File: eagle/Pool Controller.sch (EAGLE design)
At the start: 23 parts, among them J1 POWER_JACKPTH, J2 Temp_Pool, J3 Relay, J4 Solar_Mon, J5 Temp_Solar

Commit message: Updated Eagle Files
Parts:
- S4: value Solar_Toggle -> Display Step
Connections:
- new net N$10: R10.2, S2.3, S2.4
- new net N$13: R8.2, S4.3, S4.4
- new net N$15: R6.2, S1.3, S1.4
- new net VCC: R4.P$1
- net 3.3V: no longer R5.1
- net GND: now also R5.1; no longer R4.P$1
- net N$8: no longer R10.2, R6.2, R8.2, S1.3, S1.4, S2.3, S2.4, S4.3, S4.4
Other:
- note added: "2.1"
- note removed: "2.0.0"
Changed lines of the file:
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@@
 <part name="S2" library="SparkFun-Retired" deviceset="TAC_SWITCH" device="PTH" value="Clean"/>
 <part name="S3" library="SparkFun-Retired" deviceset="TAC_SWITCH" device="PTH" value="Stop"/>
-<part name="S4" library="SparkFun-Retired" deviceset="TAC_SWITCH" device="PTH" value="Solar_Toggle"/>
+<part name="S4" library="SparkFun-Retired" deviceset="TAC_SWITCH" device="PTH" value="Display Step"/>
 <part name="R10" library="SparkFun-Passives" deviceset="RESISTOR" device="AXIAL-0.3" value="22KΩ"/>
 <part name="J3" library="SparkFun-Connectors" deviceset="M06" device="SILK_FEMALE_PTH" value="Relay"/>
@@
 <sheet>
 <plain>
-<text x="233.68" y="-38.1" size="1.778" layer="97">2.0.0</text>
+<text x="233.68" y="-38.1" size="1.778" layer="97">2.1</text>
 </plain>
 <instances>
@@
 <instance part="GND4" gate="1" x="182.88" y="40.64" rot="R180"/>
 <instance part="SUPPLY4" gate="G$1" x="132.08" y="43.18"/>
-<instance part="SUPPLY5" gate="G$1" x="53.34" y="55.88"/>
-<instance part="GND6" gate="1" x="53.34" y="68.58"/>
+<instance part="SUPPLY5" gate="G$1" x="53.34" y="73.66"/>
+<instance part="GND6" gate="1" x="53.34" y="50.8"/>
 <instance part="SUPPLY6" gate="G$1" x="27.94" y="127"/>
 <instance part="SUPPLY7" gate="G$1" x="187.96" y="38.1"/>
@@
 </segment>
 <segment>
-<pinref part="GND6" gate="1" pin="GND"/>
-<pinref part="R4" gate="G$1" pin="P$1"/>
-<wire x1="53.34" y1="71.12" x2="60.96" y2="71.12" width="0.1524" layer="91"/>
-</segment>
-<segment>
 <pinref part="U$1" gate="G$1" pin="GND@21"/>
 <wire x1="165.1" y1="93.98" x2="180.34" y2="93.98" width="0.1524" layer="91"/>
@@
 <pinref part="J5" gate="G$1" pin="2"/>
 <wire x1="96.52" y1="73.66" x2="93.98" y2="73.66" width="0.1524" layer="91"/>
+</segment>
+<segment>
+<pinref part="R5" gate="G$1" pin="1"/>
+<wire x1="60.96" y1="55.88" x2="53.34" y2="55.88" width="0.1524" layer="91"/>
+<pinref part="GND6" gate="1" pin="GND"/>
+<wire x1="53.34" y1="55.88" x2="53.34" y2="53.34" width="0.1524" layer="91"/>
 </segment>
 </net>
@@
 <net name="N$8" class="0">
 <segment>
-<pinref part="R8" gate="G$1" pin="2"/>
 <pinref part="R7" gate="G$1" pin="2"/>
-<wire x1="114.3" y1="-17.78" x2="114.3" y2="0" width="0.1524" layer="91"/>
-<pinref part="R6" gate="G$1" pin="2"/>
-<wire x1="114.3" y1="0" x2="114.3" y2="20.32" width="0.1524" layer="91"/>
-<junction x="114.3" y="0"/>
-<pinref part="R10" gate="G$1" pin="2"/>
-<wire x1="114.3" y1="20.32" x2="114.3" y2="38.1" width="0.1524" layer="91"/>
-<junction x="114.3" y="20.32"/>
-<pinref part="S2" gate="S" pin="4"/>
-<wire x1="109.22" y1="17.78" x2="111.76" y2="17.78" width="0.1524" layer="91"/>
-<wire x1="111.76" y1="17.78" x2="111.76" y2="20.32" width="0.1524" layer="91"/>
-<wire x1="111.76" y1="20.32" x2="114.3" y2="20.32" width="0.1524" layer="91"/>
-<pinref part="S2" gate="S" pin="3"/>
-<wire x1="109.22" y1="20.32" x2="111.76" y2="20.32" width="0.1524" layer="91"/>
-<junction x="111.76" y="20.32"/>
-<pinref part="S1" gate="S" pin="4"/>
-<wire x1="109.22" y1="35.56" x2="111.76" y2="35.56" width="0.1524" layer="91"/>
-<wire x1="111.76" y1="35.56" x2="111.76" y2="38.1" width="0.1524" layer="91"/>
-<wire x1="111.76" y1="38.1" x2="114.3" y2="38.1" width="0.1524" layer="91"/>
-<junction x="114.3" y="38.1"/>
-<pinref part="S1" gate="S" pin="3"/>
-<wire x1="109.22" y1="38.1" x2="111.76" y2="38.1" width="0.1524" layer="91"/>
-<junction x="111.76" y="38.1"/>
 <pinref part="S3" gate="S" pin="4"/>
 <wire x1="109.22" y1="-2.54" x2="111.76" y2="-2.54" width="0.1524" layer="91"/>
@@
 <wire x1="109.22" y1="0" x2="111.76" y2="0" width="0.1524" layer="91"/>
 <junction x="111.76" y="0"/>
-<pinref part="S4" gate="S" pin="4"/>
-<wire x1="109.22" y1="-20.32" x2="111.76" y2="-20.32" width="0.1524" layer="91"/>
-<wire x1="111.76" y1="-20.32" x2="111.76" y2="-17.78" width="0.1524" layer="91"/>
-<wire x1="111.76" y1="-17.78" x2="114.3" y2="-17.78" width="0.1524" layer="91"/>
-<junction x="114.3" y="-17.78"/>
-<pinref part="S4" gate="S" pin="3"/>
-<wire x1="109.22" y1="-17.78" x2="111.76" y2="-17.78" width="0.1524" layer="91"/>
-<junction x="111.76" y="-17.78"/>
 </segment>
 </net>
@@
 </segment>
 <segment>
-<pinref part="R5" gate="G$1" pin="1"/>
-<pinref part="SUPPLY5" gate="G$1" pin="VCC"/>
-<wire x1="60.96" y1="55.88" x2="53.34" y2="55.88" width="0.1524" layer="91"/>
-</segment>
-<segment>
 <pinref part="SUPPLY10" gate="G$1" pin="VCC"/>
 <wire x1="213.36" y1="104.14" x2="213.36" y2="96.52" width="0.1524" layer="91"/>
@@
 </segment>
 </net>
+<net name="VCC" class="0">
+<segment>
+<pinref part="R4" gate="G$1" pin="P$1"/>
+<wire x1="60.96" y1="71.12" x2="53.34" y2="71.12" width="0.1524" layer="91"/>
+<pinref part="SUPPLY5" gate="G$1" pin="VCC"/>
+<wire x1="53.34" y1="71.12" x2="53.34" y2="73.66" width="0.1524" layer="91"/>
+</segment>
+</net>
+<net name="N$15" class="0">
+<segment>
+<pinref part="R6" gate="G$1" pin="2"/>
+<wire x1="111.76" y1="38.1" x2="114.3" y2="38.1" width="0.1524" layer="91"/>
+<pinref part="S1" gate="S" pin="3"/>
+<wire x1="109.22" y1="38.1" x2="111.76" y2="38.1" width="0.1524" layer="91"/>
+<junction x="111.76" y="38.1"/>
+<wire x1="111.76" y1="35.56" x2="111.76" y2="38.1" width="0.1524" layer="91"/>
+<pinref part="S1" gate="S" pin="4"/>
+<wire x1="109.22" y1="35.56" x2="111.76" y2="35.56" width="0.1524" layer="91"/>
+</segment>
+</net>
+<net name="N$10" class="0">
+<segment>
+<pinref part="R10" gate="G$1" pin="2"/>
+<wire x1="111.76" y1="20.32" x2="114.3" y2="20.32" width="0.1524" layer="91"/>
+<pinref part="S2" gate="S" pin="3"/>
+<wire x1="109.22" y1="20.32" x2="111.76" y2="20.32" width="0.1524" layer="91"/>
+<junction x="111.76" y="20.32"/>
+<wire x1="111.76" y1="17.78" x2="111.76" y2="20.32" width="0.1524" layer="91"/>
+<pinref part="S2" gate="S" pin="4"/>
+<wire x1="109.22" y1="17.78" x2="111.76" y2="17.78" width="0.1524" layer="91"/>
+</segment>
+</net>
+<net name="N$13" class="0">
+<segment>
+<pinref part="R8" gate="G$1" pin="2"/>
+<wire x1="111.76" y1="-17.78" x2="114.3" y2="-17.78" width="0.1524" layer="91"/>
+<pinref part="S4" gate="S" pin="3"/>
+<wire x1="109.22" y1="-17.78" x2="111.76" y2="-17.78" width="0.1524" layer="91"/>
+<junction x="111.76" y="-17.78"/>
+<wire x1="111.76" y1="-20.32" x2="111.76" y2="-17.78" width="0.1524" layer="91"/>
+<pinref part="S4" gate="S" pin="4"/>
+<wire x1="109.22" y1="-20.32" x2="111.76" y2="-20.32" width="0.1524" layer="91"/>
+</segment>
+</net>

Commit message: Finished initial design
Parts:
- renumbered U$1 to POOL_CONTROLLER
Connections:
- removed net VCC: R4.P$1
- net 3.3V: now also R4.P$1
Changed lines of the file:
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@@
 </classes>
 <parts>
-<part name="U$1" library="Spark" deviceset="PHOTON" device="_WITH_HEADERS"/>
+<part name="POOL_CONTROLLER" library="Spark" deviceset="PHOTON" device="_WITH_HEADERS"/>
 <part name="U$2" library="tft_1.8_1.44_oled_0.96" deviceset="OLED_0.96_I2C" device=""/>
 <part name="FRAME1" library="frames" deviceset="LETTER_L" device=""/>
@@
 </plain>
 <instances>
-<instance part="U$1" gate="G$1" x="147.32" y="81.28"/>
+<instance part="POOL_CONTROLLER" gate="G$1" x="147.32" y="81.28"/>
 <instance part="U$2" gate="G$1" x="177.8" y="20.32" rot="R180"/>
 <instance part="FRAME1" gate="G$1" x="-5.08" y="-45.72"/>
@@
 </segment>
 <segment>
-<pinref part="U$1" gate="G$1" pin="GND@21"/>
+<pinref part="POOL_CONTROLLER" gate="G$1" pin="GND@21"/>
 <wire x1="165.1" y1="93.98" x2="180.34" y2="93.98" width="0.1524" layer="91"/>
 <wire x1="180.34" y1="93.98" x2="180.34" y2="99.06" width="0.1524" layer="91"/>
@@
 </segment>
 <segment>
-<pinref part="U$1" gate="G$1" pin="GND@2"/>
+<pinref part="POOL_CONTROLLER" gate="G$1" pin="GND@2"/>
 <pinref part="GND2" gate="1" pin="GND"/>
 <wire x1="129.54" y1="104.14" x2="121.92" y2="104.14" width="0.1524" layer="91"/>
@@
 <net name="N$3" class="0">
 <segment>
-<pinref part="U$1" gate="G$1" pin="D0"/>
+<pinref part="POOL_CONTROLLER" gate="G$1" pin="D0"/>
 <wire x1="165.1" y1="53.34" x2="175.26" y2="53.34" width="0.1524" layer="91"/>
 <pinref part="U$2" gate="G$1" pin="SDA"/>
@@
 <net name="N$4" class="0">
 <segment>
-<pinref part="U$1" gate="G$1" pin="D1"/>
+<pinref part="POOL_CONTROLLER" gate="G$1" pin="D1"/>
 <wire x1="165.1" y1="58.42" x2="177.8" y2="58.42" width="0.1524" layer="91"/>
 <pinref part="U$2" gate="G$1" pin="SCL"/>
@@
 <net name="N$5" class="0">
 <segment>
-<pinref part="U$1" gate="G$1" pin="A1"/>
+<pinref part="POOL_CONTROLLER" gate="G$1" pin="A1"/>
 <wire x1="129.54" y1="58.42" x2="76.2" y2="58.42" width="0.1524" layer="91"/>
 <pinref part="R4" gate="G$1" pin="P$2"/>
@@
 <net name="N$1" class="0">
 <segment>
-<pinref part="U$1" gate="G$1" pin="D2"/>
+<pinref part="POOL_CONTROLLER" gate="G$1" pin="D2"/>
 <wire x1="165.1" y1="63.5" x2="213.36" y2="63.5" width="0.1524" layer="91"/>
 <wire x1="213.36" y1="63.5" x2="213.36" y2="66.04" width="0.1524" layer="91"/>
@@
 <net name="N$2" class="0">
 <segment>
-<pinref part="U$1" gate="G$1" pin="D3"/>
+<pinref part="POOL_CONTROLLER" gate="G$1" pin="D3"/>
 <wire x1="165.1" y1="68.58" x2="218.44" y2="68.58" width="0.1524" layer="91"/>
 <pinref part="J3" gate="G$1" pin="4"/>
@@
 <net name="N$7" class="0">
 <segment>
-<pinref part="U$1" gate="G$1" pin="D5"/>
+<pinref part="POOL_CONTROLLER" gate="G$1" pin="D5"/>
 <wire x1="165.1" y1="78.74" x2="213.36" y2="78.74" width="0.1524" layer="91"/>
 <wire x1="213.36" y1="78.74" x2="213.36" y2="73.66" width="0.1524" layer="91"/>
@@
 <net name="N$9" class="0">
 <segment>
-<pinref part="U$1" gate="G$1" pin="D6"/>
+<pinref part="POOL_CONTROLLER" gate="G$1" pin="D6"/>
 <wire x1="165.1" y1="83.82" x2="213.36" y2="83.82" width="0.1524" layer="91"/>
 <wire x1="213.36" y1="83.82" x2="213.36" y2="93.98" width="0.1524" layer="91"/>
@@
 <wire x1="96.52" y1="38.1" x2="96.52" y2="53.34" width="0.1524" layer="91"/>
 <junction x="96.52" y="38.1"/>
-<pinref part="U$1" gate="G$1" pin="A0"/>
+<pinref part="POOL_CONTROLLER" gate="G$1" pin="A0"/>
 <wire x1="96.52" y1="53.34" x2="129.54" y2="53.34" width="0.1524" layer="91"/>
 </segment>
@@
 <pinref part="J3" gate="G$1" pin="3"/>
 <wire x1="210.82" y1="71.12" x2="218.44" y2="71.12" width="0.1524" layer="91"/>
-<pinref part="U$1" gate="G$1" pin="D4"/>
+<pinref part="POOL_CONTROLLER" gate="G$1" pin="D4"/>
 <wire x1="165.1" y1="73.66" x2="210.82" y2="73.66" width="0.1524" layer="91"/>
 </segment>
@@
 <wire x1="104.14" y1="71.12" x2="111.76" y2="71.12" width="0.1524" layer="91"/>
 <wire x1="111.76" y1="71.12" x2="111.76" y2="63.5" width="0.1524" layer="91"/>
-<pinref part="U$1" gate="G$1" pin="A2"/>
+<pinref part="POOL_CONTROLLER" gate="G$1" pin="A2"/>
 <wire x1="111.76" y1="63.5" x2="129.54" y2="63.5" width="0.1524" layer="91"/>
 <pinref part="R14" gate="G$1" pin="2"/>
@@
 <segment>
 <wire x1="114.3" y1="86.36" x2="114.3" y2="68.58" width="0.1524" layer="91"/>
-<pinref part="U$1" gate="G$1" pin="A3"/>
+<pinref part="POOL_CONTROLLER" gate="G$1" pin="A3"/>
 <wire x1="114.3" y1="68.58" x2="129.54" y2="68.58" width="0.1524" layer="91"/>
 <pinref part="J2" gate="G$1" pin="1"/>
@@
 </segment>
 <segment>
-<pinref part="U$1" gate="G$1" pin="3V3"/>
+<pinref part="POOL_CONTROLLER" gate="G$1" pin="3V3"/>
 <wire x1="165.1" y1="109.22" x2="175.26" y2="109.22" width="0.1524" layer="91"/>
 <pinref part="SUPPLY2" gate="G$1" pin="VCC"/>
@@
 <wire x1="104.14" y1="101.6" x2="104.14" y2="106.68" width="0.1524" layer="91"/>
 </segment>
-</net>
-<net name="VCC" class="0">
 <segment>
 <pinref part="R4" gate="G$1" pin="P$1"/>

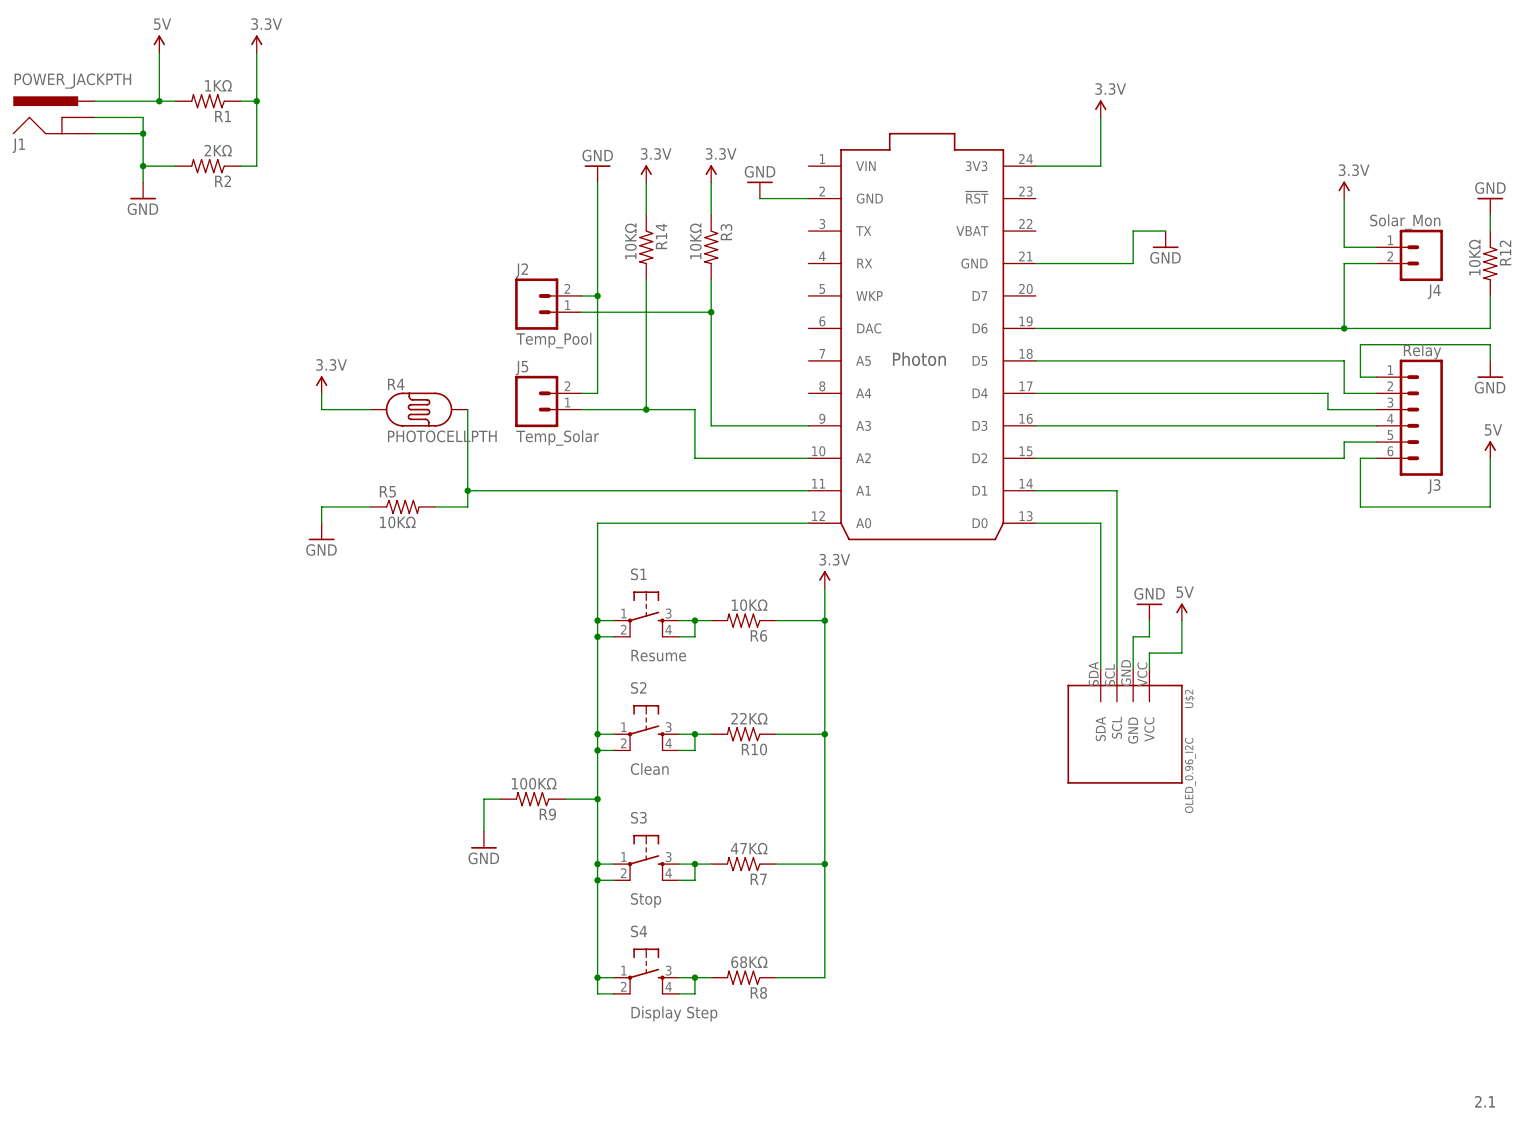
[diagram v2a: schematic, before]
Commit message: Updated Eagle files for PCB v2.1
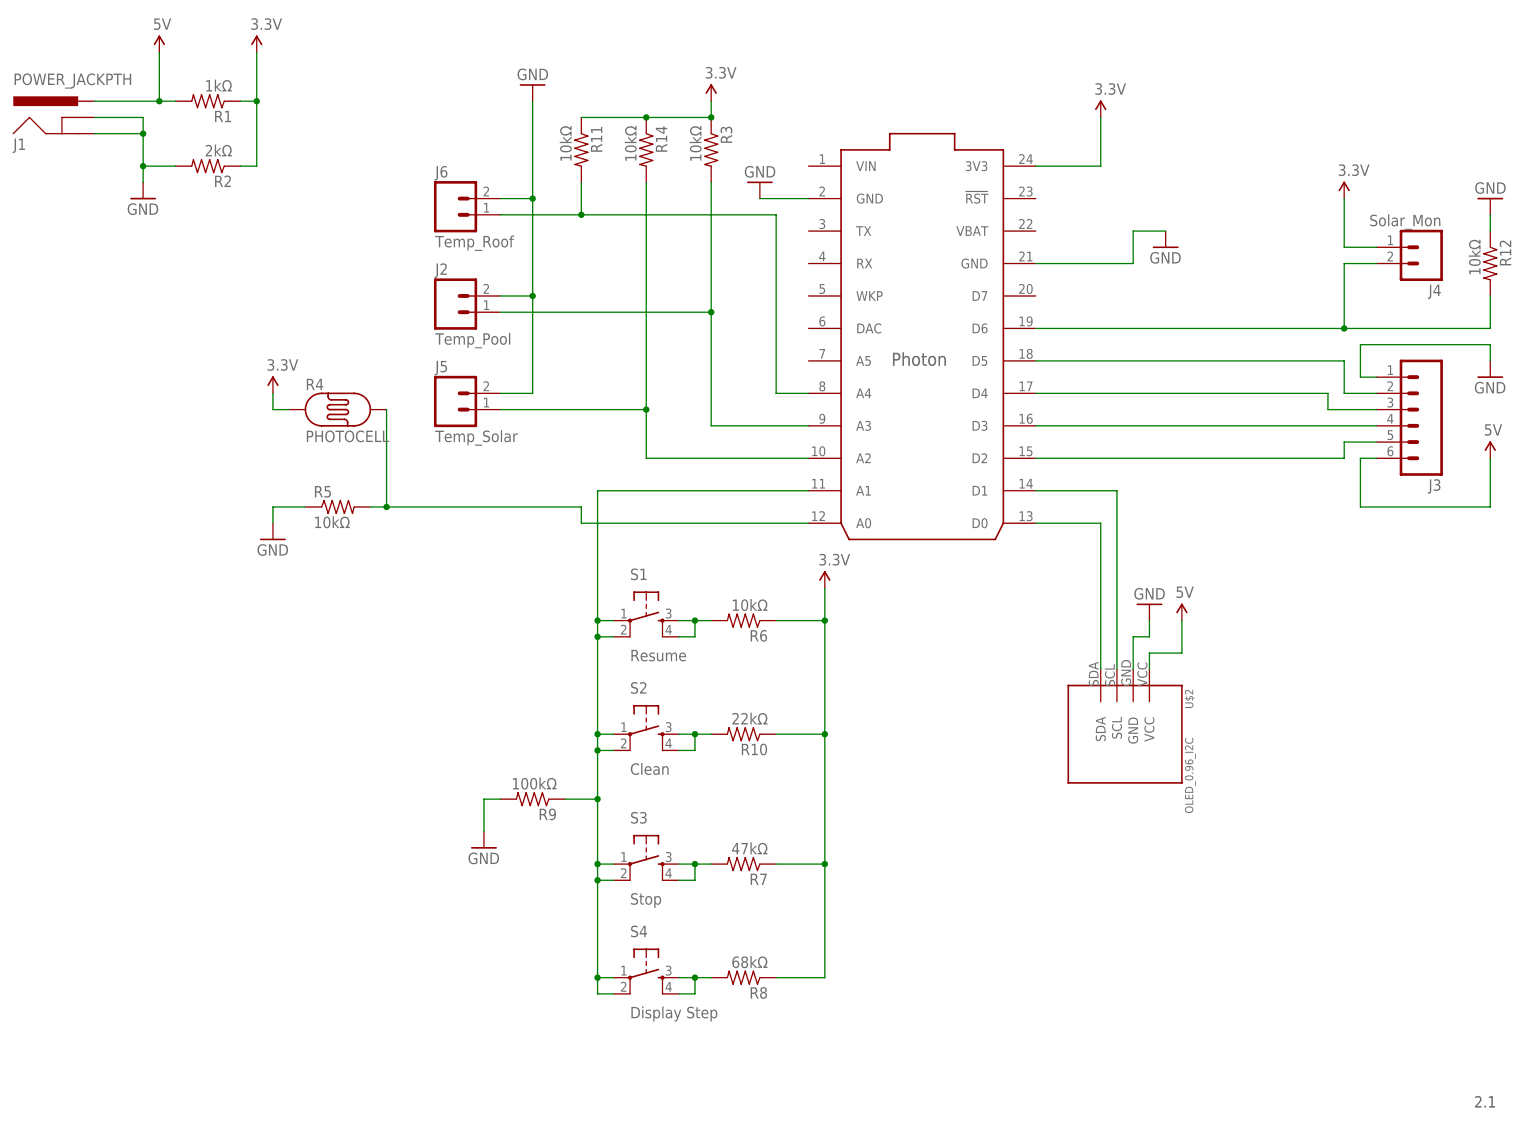
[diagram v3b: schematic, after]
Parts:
- added J6: Temp_Roof, SparkFun-Connectors:M025MM
- added R11: 10kΩ, SparkFun-Passives:RESISTORAXIAL-0.3
- J3: value Relay -> (none)
- R1: value 1KΩ -> 1kΩ
- R10: value 22KΩ -> 22kΩ
- R12, R14, R3, R5, R6: value 10KΩ -> 10kΩ
- R2: value 2KΩ -> 2kΩ
- R4: value PHOTOCELLPTH -> PHOTOCELL
- R7: value 47KΩ -> 47kΩ
- R8: value 68KΩ -> 68kΩ
- R9: value 100KΩ -> 100kΩ
- renumbered POOL_CONTROLLER to PHOTON
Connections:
- new net N$17: J6.1, PHOTON.A4, R11.2
- net 3.3V: now also R11.1
- net GND: now also J6.2
- net N$14: now also PHOTON.A1; no longer PHOTON.A0
- net N$5: now also PHOTON.A0; no longer PHOTON.A1
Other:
- moved on the sheet: J2, J5, R14, R3, R4, R5
